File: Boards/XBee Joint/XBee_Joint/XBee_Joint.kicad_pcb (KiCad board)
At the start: 4 copper layers, 67.4 x 98.5 mm, 63 parts, among them J1 Conn_01x07, J2 USB_C_Receptacle_USB2.0, Q1 Q_NMOS_GSD, SW2 SLIDE, U1 MCU_RaspberryPi_RP2040_RP2040, U2 XBee_SMT, U3 W25Q128JVS, U4 USBLC6-2SC6, U5 TPS63021DSJR, U6 LT6703CDC-3, U7 TVS1800DRVR, U8 TPS2121RUXR, Y1 12MHz

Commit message: working on xbee joint
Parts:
- removed BT1: 1S1P LiPo, BITSv5:1042_KEY
- removed C19, C21, C22: 1uF, Capacitor_SMD:C_0603_1608Metric_Pad1.08x0.95mm_HandSolder
- removed C20, C23, C24, C25: 10uF, Capacitor_SMD:C_0603_1608Metric_Pad1.08x0.95mm_HandSolder
- removed C26: 100nF, Capacitor_SMD:C_0603_1608Metric_Pad1.08x0.95mm_HandSolder
- removed C27, C28, C29: 22uF, Capacitor_SMD:C_0603_1608Metric_Pad1.08x0.95mm_HandSolder
- removed L1: 1.5uH, Inductor_SMD:L_Coilcraft_XxL4040
- removed R11: 1.05M, Resistor_SMD:R_0603_1608Metric_Pad0.98x0.95mm_HandSolder
- removed R12: 154K, Resistor_SMD:R_0603_1608Metric_Pad0.98x0.95mm_HandSolder
- removed R13: 46.4K, Resistor_SMD:R_0603_1608Metric_Pad0.98x0.95mm_HandSolder
- removed R14, R15, R16: 10K, Resistor_SMD:R_0603_1608Metric_Pad0.98x0.95mm_HandSolder
- removed R17: 22K, Resistor_SMD:R_0603_1608Metric_Pad0.98x0.95mm_HandSolder
- removed R18: 510K, Resistor_SMD:R_0603_1608Metric_Pad0.98x0.95mm_HandSolder
- removed SW2: SLIDE, BITSv5:CL-SB-12B-01_NDC
- removed U5: TPS63021DSJR, BITSv5:IC_TPS63021DSJR
- removed U7: TVS1800DRVR, BITSv5:TVS1800
- removed U8: TPS2121RUXR, BITSv5:TPS2121
- C1, C11, C5, C6, J2, R1: moved to F.Cu
- U6: value LT6703CDC-3 -> AP7361C-33E; footprint BITSv5:DFN-3_DC_LIT -> Package_TO_SOT_SMD:SOT-223-3_TabPin2
- moved U2 140.2 mm to (241.9, 46.7)
- moved U4 126.3 mm to (206.0, 49.3), turned to 0 degrees
- moved SW1 100.2 mm to (206.7, 42.6), turned to 0 degrees
- moved U6 96.7 mm to (155.6, 47.2), turned to 0 degrees
- moved R8 93.0 mm to (150.0, 39.3), turned to 0 degrees
- moved R7 90.0 mm to (150.0, 36.8), turned to 0 degrees
- moved D1 86.2 mm to (154.2, 41.1)
- moved R9 83.8 mm to (150.0, 41.8), turned to 0 degrees
- moved J2 82.7 mm to (141.9, 44.6), turned to 0 degrees
- moved U3 82.2 mm to (157.3, 36.4), turned to 0 degrees
- moved C16 77.2 mm to (141.3, 41.8), turned to 0 degrees
- moved R5 72.2 mm to (150.0, 34.3), turned to 0 degrees
- moved Q1 65.0 mm to (141.7, 56.5), turned to 0 degrees
- moved R1 63.7 mm to (145.6, 39.3), turned to 0 degrees
- moved C17 62.6 mm to (145.6, 34.3), turned to 0 degrees
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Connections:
- net /USB_D+ renamed /D+
- net /USB_D- renamed /D-
- net /XIN renamed Net-(U1-XIN)
- net /XOUT renamed Net-(U1-XOUT)
- U6 pad 1: Net-(SW2-C) -> VBUS
- U6 pad 2: VCC -> GND
- U6 pad 3: Net-(U6-IN+) -> +3V3
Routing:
- net GND: track 78.6 -> 1.27 mm, vias 68 -> 0
- net /XBEE_DOUT: track 73.3 -> 0.00 mm
- net /XBEE_DIN: track 71.6 -> 0.00 mm
- net /XBEE_RTS: track 68.5 -> 0.00 mm
- net /LVC_CUTOFF: track 47.2 -> 0.00 mm, vias 2 -> 0
- net /RP_SWD: track 41.1 -> 0.00 mm, vias 1 -> 0
- net /RP_SWCLK: track 32.5 -> 0.00 mm, vias 1 -> 0
- net /XBEE_DTR: track 28.2 -> 0.00 mm
- net Net-(SW2-C): track 27.2 -> 0.00 mm
- net /LED: track 21.4 -> 0.00 mm, vias 2 -> 0
- net +3V3: track 34.1 -> 13.6 mm, vias 18 -> 0
- net /QSPI_SS: track 19.4 -> 0.00 mm
- net /QSPI_SD3: track 19.3 -> 0.00 mm
- net /D-: track 18.3 -> 0.00 mm
- net /D+: track 18.2 -> 0.00 mm
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- added copper zone on F.Cu, net +1V1
- removed copper zone on In2.Cu, net +3V3
- removed copper zone on F.Cu, net +BATT
- removed copper zone on In2.Cu, net +BATT
- removed copper zone on F.Cu, net GND
- removed copper zone on In1.Cu, net GND
- removed copper zone on F.Cu, net Net-(U5-L1_8)
- removed copper zone on F.Cu, net Net-(U5-L2_6)
- removed copper zone on F.Cu, net VBUS
- removed copper zone on In2.Cu, net VBUS
- removed copper zone on F.Cu, net VCC
- removed copper zone on In2.Cu, net VCC
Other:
- board outline removed
- board text removed: "J. Bishop, M. Shipman, A. Takeuchi"
- board text removed: "XBee Joint"

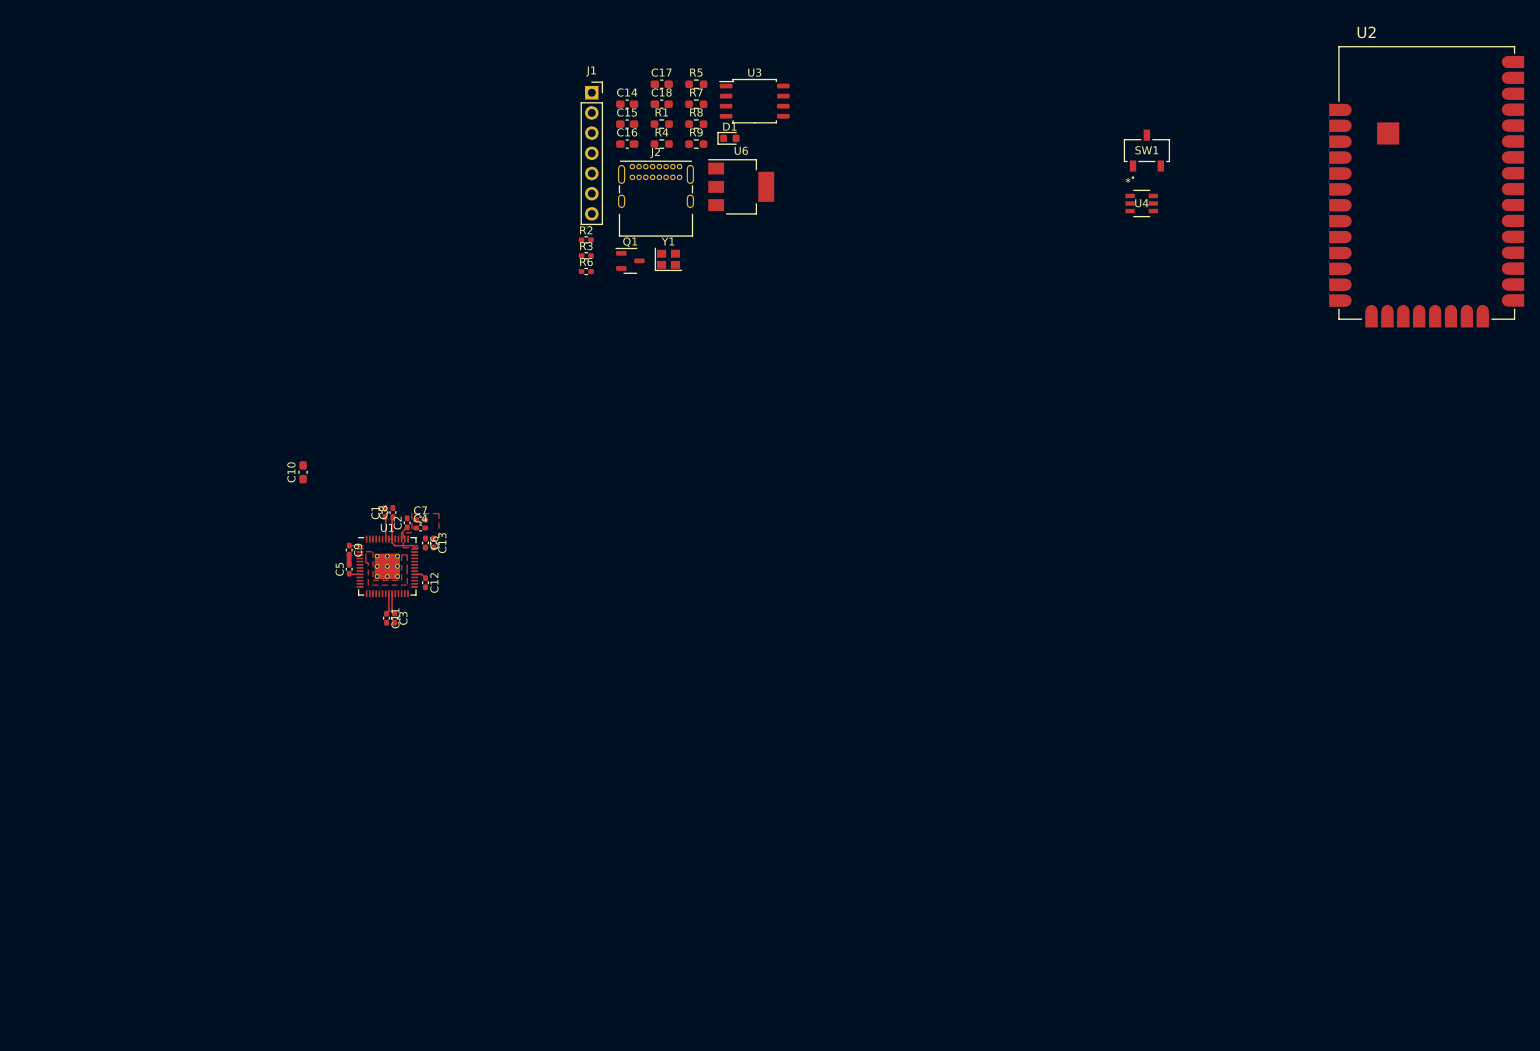
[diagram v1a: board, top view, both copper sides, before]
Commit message: xbee joint layout almost complete
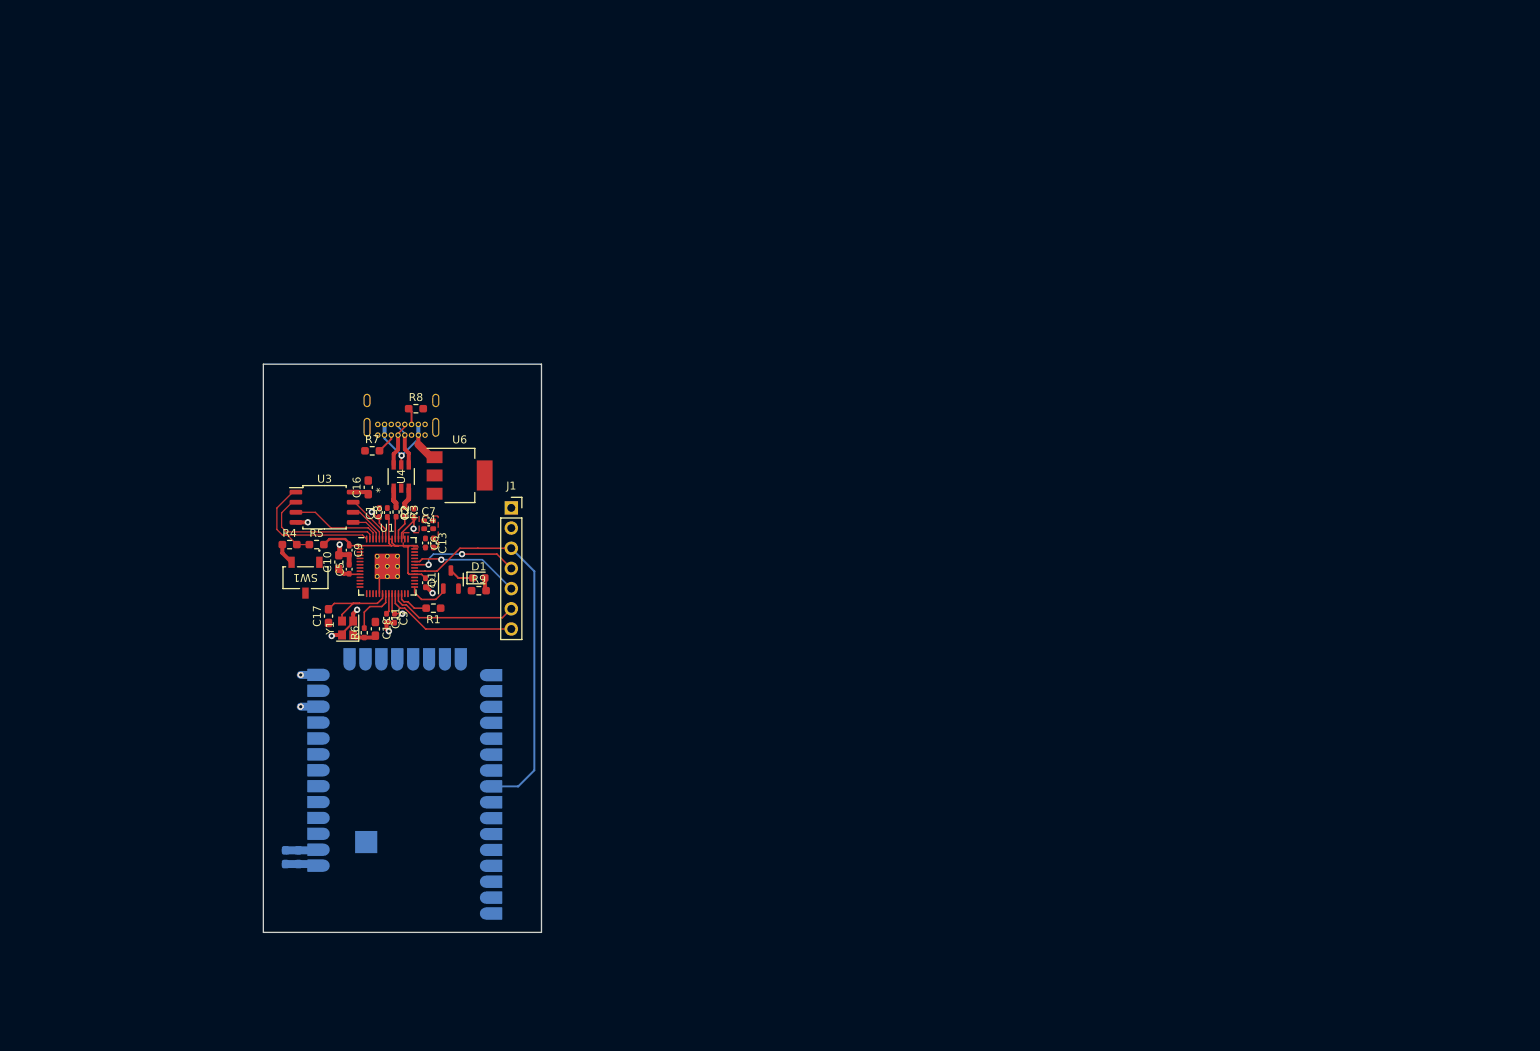
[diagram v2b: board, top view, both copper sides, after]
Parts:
- C14, C15, J2, U2: moved to B.Cu
- moved U2 149.7 mm to (113.3, 123.4)
- moved SW1 118.7 mm to (100.8, 96.4), turned to 180 degrees
- moved C14 104.1 mm to (98.3, 131.5), turned to -90 degrees
- moved C15 101.1 mm to (99.9, 131.5), turned to -90 degrees
- moved U4 99.3 mm to (112.8, 83.6), turned to 90 degrees
- moved C17 79.0 mm to (103.7, 101.2), turned to 90 degrees
- moved C18 75.2 mm to (109.6, 102.8), turned to -90 degrees
- moved R5 75.1 mm to (102.2, 92.2)
- moved U3 74.4 mm to (103.2, 87.5)
- moved R4 68.8 mm to (98.8, 92.2)
- moved R1 67.3 mm to (116.9, 100.2), turned to 180 degrees
- moved D1 63.7 mm to (122.6, 96.4)
- moved R9 62.5 mm to (122.6, 98.0)
- moved Y1 61.5 mm to (106.1, 102.7), turned to 90 degrees
- moved R7 59.7 mm to (109.2, 80.4)
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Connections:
- net Net-(U1-XIN) renamed /XIN
- net Net-(U1-XOUT) renamed /XOUT
- R9 pad 1: VCC -> +3V3
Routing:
- net /XBEE_RTS: track 0.00 -> 48.5 mm
- net GND: track 1.27 -> 25.6 mm, vias 0 -> 8
- net +3V3: track 13.6 -> 35.3 mm
- net /QSPI_SS: track 0.00 -> 21.6 mm
- net +1V1: track 7.21 -> 25.5 mm, vias 0 -> 3
- net /RP_SWCLK: track 0.00 -> 17.2 mm
- net /RP_SWD: track 0.00 -> 16.5 mm
- net /QSPI_SD1: track 0.00 -> 16.2 mm
- net VBUS: track 0.00 -> 14.7 mm, vias 0 -> 1
- net /XBEE_DIN: track 0.00 -> 13.9 mm, vias 0 -> 2
- net /XBEE_DOUT: track 0.00 -> 13.9 mm, vias 0 -> 1
- net /QSPI_SD2: track 0.00 -> 11.6 mm
- net /XIN: track 0.00 -> 11.6 mm
- net /XOUT: track 0.00 -> 6.32 mm
- net /QSPI_SD3: track 0.00 -> 6.26 mm
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- added copper zone on In1.Cu, net +1V1
- added copper zone on In1.Cu, net GND
- added copper zone on In2.Cu, net GND
- removed copper zone on F.Cu, net +1V1
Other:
- board outline added: 35 x 71.5 mm

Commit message: updates
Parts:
- removed U6: AP7361C-33E, Package_TO_SOT_SMD:SOT-223-3_TabPin2
- added R10: 166k, Resistor_SMD:R_0603_1608Metric_Pad0.98x0.95mm_HandSolder, F.Cu at (131.1, 88.3)
- added R11: 100k, Resistor_SMD:R_0603_1608Metric_Pad0.98x0.95mm_HandSolder, F.Cu at (134.6, 88.3)
- added R12: 330, Resistor_SMD:R_1210_3225Metric_Pad1.30x2.65mm_HandSolder, F.Cu at (118.0, 84.4)
- added U7: MIC29302WU, Package_TO_SOT_SMD:TO-263-5_TabPin3, B.Cu at (110.3, 93.0)
- moved J1 12.0 mm to (138.7, 87.7)
- moved R8 6.38 mm to (108.5, 73.8)
- moved J2 6.25 mm to (103.7, 78.4)
- moved R7 6.25 mm to (103.0, 80.4)
- moved R9 1.60 mm to (122.7, 99.6)
- moved D1 1.60 mm to (122.6, 98.0)
- moved Q1 0.61 mm to (119.2, 97.2)
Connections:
- U2 pad 10: /XBEE_DTR -> /XBEE_PRO_DTR
- U2 pad 29: /XBEE_RTS -> /XBEE_PRO_RTS
- U2 pad 3: /XBEE_DOUT -> /XBEE_PRO_DOUT
- U2 pad 4: /XBEE_DIN -> /XBEE_PRO_DIN
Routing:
- net /XBEE_RTS: track 48.5 -> 25.5 mm
- net /RP_SWCLK: track 17.2 -> 29.2 mm
- net /XBEE_DOUT: track 13.9 -> 25.9 mm
- net /XBEE_DIN: track 13.9 -> 25.9 mm
- net /RP_SWD: track 16.5 -> 28.4 mm
- net VBUS: track 14.7 -> 4.20 mm
- net GND: track 25.6 -> 32.9 mm, vias 8 -> 11
- net Net-(J2-D--PadA7): track 5.66 -> 11.6 mm
- net /XBEE_PRO_RTS: track 0.00 -> 5.91 mm
- net Net-(U7-ADJ): track 0.00 -> 5.74 mm
- net Net-(J2-D+-PadA6): track 5.68 -> 10.7 mm
- net +3V3: track 35.3 -> 39.3 mm
- net Net-(J2-CC2): track 2.13 -> 3.43 mm
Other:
- board size 35 x 71.5 mm -> 51.7 x 71.5 mm

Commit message: dorji joint?
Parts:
- removed Q1: Q_NMOS_GSD, Package_TO_SOT_SMD:SOT-23-3
- removed R11: 100k, Resistor_SMD:R_0603_1608Metric_Pad0.98x0.95mm_HandSolder
- removed R12: 330, Resistor_SMD:R_1210_3225Metric_Pad1.30x2.65mm_HandSolder
- removed R5: 10K, Resistor_SMD:R_0603_1608Metric_Pad0.98x0.95mm_HandSolder
- removed SW1: ~, BITSv5:CAS-120TB_NDC-M
- removed U7: MIC29302WU, Package_TO_SOT_SMD:TO-263-5_TabPin3
- added AE1: Antenna, Connector_Coaxial:SMA_Molex_73251-1153_EdgeMount_Horizontal, B.Cu at (73.3, 107.1)
- added H1: M2, MountingHole:MountingHole_2.2mm_M2_Pad, F.Cu at (69.3, 147.0)
- added H2: M2, MountingHole:MountingHole_2.2mm_M2_Pad, F.Cu at (88.3, 105.0)
- added SW2: ~, BITSv5:CAS-120TB_NDC-M, F.Cu at (86.8, 116.2)
- added U5: USBLC6-2SC6, BITSv5:SOT23-6L_STM, F.Cu at (77.4, 138.9)
- C1, C11, C12, C13, C7, C8, C9: footprint Capacitor_SMD:C_0402_1005Metric_Pad0.74x0.62mm_HandSolder -> Capacitor_SMD:C_0402_1005Metric
- C10: value 10uF -> 100nF; footprint Capacitor_SMD:C_0603_1608Metric_Pad1.08x0.95mm_HandSolder -> Capacitor_SMD:C_0402_1005Metric
- C14: value 1uF -> 100nF; footprint Capacitor_SMD:C_0603_1608Metric_Pad1.08x0.95mm_HandSolder -> Capacitor_SMD:C_0402_1005Metric; moved to F.Cu
- C15: value 100pF -> 100nF; footprint Capacitor_SMD:C_0603_1608Metric_Pad1.08x0.95mm_HandSolder -> Capacitor_SMD:C_0402_1005Metric; moved to F.Cu
- C16: value 100nF -> 1uF; footprint Capacitor_SMD:C_0603_1608Metric_Pad1.08x0.95mm_HandSolder -> Capacitor_SMD:C_0603_1608Metric
- C17: value 10pF -> 100nF; footprint Capacitor_SMD:C_0603_1608Metric_Pad1.08x0.95mm_HandSolder -> Capacitor_SMD:C_0603_1608Metric
- C18: value 10pF -> 10uF; footprint Capacitor_SMD:C_0603_1608Metric_Pad1.08x0.95mm_HandSolder -> Capacitor_SMD:C_0603_1608Metric
- C2: value 100nF -> 10pF; footprint Capacitor_SMD:C_0402_1005Metric_Pad0.74x0.62mm_HandSolder -> Capacitor_SMD:C_0402_1005Metric
- C3: value 1uF -> 10pF; footprint Capacitor_SMD:C_0402_1005Metric_Pad0.74x0.62mm_HandSolder -> Capacitor_SMD:C_0402_1005Metric
- C4: value 1uF -> 100nF; footprint Capacitor_SMD:C_0402_1005Metric_Pad0.74x0.62mm_HandSolder -> Capacitor_SMD:C_0402_1005Metric
- C5, C6: value 100nF -> 1uF; footprint Capacitor_SMD:C_0402_1005Metric_Pad0.74x0.62mm_HandSolder -> Capacitor_SMD:C_0402_1005Metric
- J1: value Conn_01x07 -> SOICbite; footprint Connector_PinSocket_2.54mm:PinSocket_1x07_P2.54mm_Vertical -> BITSv5:SOIC_clipProgSmall
- J2: footprint Connector_USB:USB_C_Receptacle_GCT_USB4085 -> Connector_USB:USB_C_Receptacle_GCT_USB4105-xx-A_16P_TopMnt_Horizontal; moved to F.Cu
- R1: value 10K -> 1K; footprint Resistor_SMD:R_0603_1608Metric_Pad0.98x0.95mm_HandSolder -> Capacitor_SMD:C_0402_1005Metric
- R10: value 166k -> 5.1K
- R2, R3: value 27Ω -> 27; footprint Resistor_SMD:R_0402_1005Metric_Pad0.72x0.64mm_HandSolder -> Resistor_SMD:R_0402_1005Metric
- R4: value 1K -> 10K; footprint Resistor_SMD:R_0603_1608Metric_Pad0.98x0.95mm_HandSolder -> Resistor_SMD:R_0603_1608Metric
- R6: value 1K -> 470; footprint Resistor_SMD:R_0402_1005Metric_Pad0.72x0.64mm_HandSolder -> Resistor_SMD:R_0603_1608Metric
- R7: value 5.1K -> 1K; footprint Resistor_SMD:R_0603_1608Metric_Pad0.98x0.95mm_HandSolder -> Resistor_SMD:R_0603_1608Metric
- R8: value 5.1K -> DNF; footprint Resistor_SMD:R_0603_1608Metric_Pad0.98x0.95mm_HandSolder -> Resistor_SMD:R_0603_1608Metric
- R9: value 470 -> 5.1K
- U2: value XBee_SMT -> AP2114H-3.3TRG1; footprint BITSv5:XCVR_XBP9X-DMUS-001 -> Package_TO_SOT_SMD:SOT-223-3_TabPin2; moved to F.Cu
- U3: value W25Q128JVS -> DRF1262TL; footprint Package_SO:SOIC-8_5.23x5.23mm_P1.27mm -> BITSv5:DRF1262TL; moved to B.Cu
- U4: value USBLC6-2SC6 -> W25Q128JVS; footprint BITSv5:SOT23-6L_STM-M -> BITSv5:WSON_128JVPIQ_WIN
- moved J1 74.8 mm to (90.4, 144.8), turned to 90 degrees
- moved J2 72.7 mm to (77.3, 146.2)
- moved R10 71.9 mm to (85.0, 143.5)
- moved D1 61.6 mm to (69.9, 129.8), turned to 90 degrees
- moved C16 59.3 mm to (84.1, 138.9), turned to -90 degrees
- moved R9 59.1 mm to (85.0, 145.2), turned to 180 degrees
- moved R8 58.2 mm to (86.0, 127.4), turned to 90 degrees
- moved R3 56.7 mm to (76.9, 131.6), turned to 90 degrees
- moved C6 56.6 mm to (74.9, 131.1)
- moved C13 56.3 mm to (82.2, 136.4), turned to 180 degrees
- moved U4 55.6 mm to (86.5, 132.5), turned to 180 degrees
- moved R2 55.2 mm to (78.2, 131.6), turned to 90 degrees
- moved C1 53.9 mm to (81.8, 134.0), turned to -90 degrees
- moved C8 52.7 mm to (74.3, 125.9), turned to -90 degrees
- moved C7 50.6 mm to (75.9, 119.6), turned to 180 degrees
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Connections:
- C16 pad 1: +3V3 -> VBUS
- C17 pad 1: GND -> VBUS
- C17 pad 2: /XIN -> GND
- C18 pad 1: GND -> VBUS
- C18 pad 2: Net-(C18-Pad2) -> GND
- C2 pad 1: +1V1 -> Net-(U1-XIN)
- C3 pad 1: +1V1 -> Net-(C3-Pad1)
- C4 pad 1: +3V3 -> +1V1
- C5 pad 1: +3V3 -> +1V1
- D1 pad 1: Net-(D1-K) -> GND
- J1 pad 1: GND -> /RP_SWCLK
- J1 pad 2: /XBEE_DTR -> /RP_SWD
- J1 pad 3: /XBEE_RTS -> unconnected-(J1-Pin_3-Pad3)
- J1 pad 4: /XBEE_DIN -> unconnected-(J1-Pin_4-Pad4)
- J1 pad 5: /XBEE_DOUT -> unconnected-(J1-Pin_5-Pad5)
- J1 pad 6: /RP_SWD -> unconnected-(J1-Pin_6-Pad6)
- J1 pad 7: /RP_SWCLK -> unconnected-(J1-Pin_7-Pad7)
- R1 pad 1: +3V3 -> Net-(C3-Pad1)
- R1 pad 2: Net-(U1-RUN) -> Net-(U1-XOUT)
- R10 pad 1: +3V3 -> Net-(J2-CC2)
- R10 pad 2: Net-(U7-ADJ) -> GND
- R2 pad 1: /D+ -> /USB_D+
- R3 pad 1: /D- -> /USB_D-
- R4 pad 1: Net-(SW1-B) -> +3V3
- R4 pad 2: /QSPI_SS -> Net-(U1-RUN)
- R6 pad 1: Net-(C18-Pad2) -> +3V3
- R6 pad 2: /XOUT -> Net-(D1-A)
- R7 pad 1: GND -> Net-(SW2-B)
- R7 pad 2: Net-(J2-CC1) -> /QSPI_SS
- R8 pad 1: Net-(J2-CC2) -> /QSPI_SS
- R8 pad 2: GND -> +3V3
- R9 pad 1: +3V3 -> GND
- R9 pad 2: Net-(D1-A) -> Net-(J2-CC1)
- U1 pad 12: unconnected-(U1-GPIO9-Pad12) -> /DRF_SW
- U1 pad 20: /XIN -> Net-(U1-XIN)
- U1 pad 21: /XOUT -> Net-(U1-XOUT)
- U1 pad 29: /LED -> /DRF_CLK
- U1 pad 3: unconnected-(U1-GPIO1-Pad3) -> /DRF_TXEN
- U1 pad 30: unconnected-(U1-GPIO19-Pad30) -> /DRF_MOSI
- U1 pad 31: unconnected-(U1-GPIO20-Pad31) -> /DRF_MISO
- U1 pad 32: unconnected-(U1-GPIO21-Pad32) -> /DRF_CS
- U1 pad 34: /XBEE_RTS -> unconnected-(U1-GPIO22-Pad34)
- U1 pad 36: /XBEE_DIN -> unconnected-(U1-GPIO24-Pad36)
- U1 pad 37: /XBEE_DOUT -> unconnected-(U1-GPIO25-Pad37)
- U1 pad 5: unconnected-(U1-GPIO3-Pad5) -> /DRF_DIO1
- U1 pad 8: unconnected-(U1-GPIO6-Pad8) -> /DRF_BUSY
- U2 pad 3: /XBEE_PRO_DOUT -> VBUS
- U3 pad 1: /QSPI_SS -> /DRF_SW
- U3 pad 2: /QSPI_SD1 -> GND
- U3 pad 3: /QSPI_SD2 -> /DRF_TXEN
- U3 pad 5: /QSPI_SD0 -> GND
- U3 pad 6: /QSPI_SCLK -> VBUS
- U3 pad 7: /QSPI_SD3 -> VBUS
- U3 pad 8: +3V3 -> /DRF_DIO1
- U4 pad 1: /D+ -> /QSPI_SS
- U4 pad 2: GND -> /QSPI_SD1
- U4 pad 3: /D- -> /QSPI_SD2
- U4 pad 4: Net-(J2-D--PadA7) -> GND
- U4 pad 5: VBUS -> /QSPI_SD0
- U4 pad 6: Net-(J2-D+-PadA6) -> /QSPI_SCLK
- Y1 pad 1: Net-(C18-Pad2) -> Net-(C3-Pad1)
- Y1 pad 3: /XIN -> Net-(U1-XIN)
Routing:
- net /XBEE_DIN: track 25.9 -> 0.00 mm, vias 2 -> 0
- net /XBEE_DOUT: track 25.9 -> 0.00 mm, vias 1 -> 0
- net /XBEE_RTS: track 25.5 -> 0.00 mm
- net VBUS: track 4.20 -> 28.5 mm, vias 1 -> 2
- net GND: track 32.9 -> 51.9 mm, vias 11 -> 82
- net /DRF_DIO1: track 0.00 -> 18.6 mm, vias 0 -> 1
- net /DRF_BUSY: track 0.00 -> 18.0 mm, vias 0 -> 1
- net /XIN: track 11.6 -> 0.00 mm
- net /DRF_MISO: track 0.00 -> 10.2 mm, vias 0 -> 1
- net /DRF_TXEN: track 0.00 -> 8.62 mm, vias 0 -> 1
- net /DRF_CS: track 0.00 -> 8.56 mm, vias 0 -> 1
- net /RP_SWD: track 28.4 -> 36.5 mm, vias 0 -> 2
- net /DRF_MOSI: track 0.00 -> 7.81 mm, vias 0 -> 1
- net Net-(J2-CC1): track 2.59 -> 9.59 mm
- net Net-(AE1-A): track 0.00 -> 6.90 mm
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- added copper zone on In1.Cu, net +3V3
- added copper zone on B.Cu, net GND
- added copper zone on F.Cu, net GND
- removed copper zone on In1.Cu, net +1V1
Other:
- board size 51.7 x 71.5 mm -> 25 x 48 mm
- board text added: "XBee Joint 10/2023 J. Bishop M. Shipman A. Takeuchi"
